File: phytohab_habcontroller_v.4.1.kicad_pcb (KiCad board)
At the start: 4 copper layers, 180.9 x 89.8 mm, 56 parts, among them J1 UMPT-02-01-L-RA-WT-M-TR, J10 I²C, J11 I²C, J12 I²C, J13 I²C, J14 I²C, J15 I²C, J2 HTSS-120-01-L-DV, J7 I²C, J8 I²C, J9 I²C, U101 DMP3037LSS-13, U301 MIC37100-3.3WS-TR, U501 DS3231M+TRL, U601 PCA9548ARGE

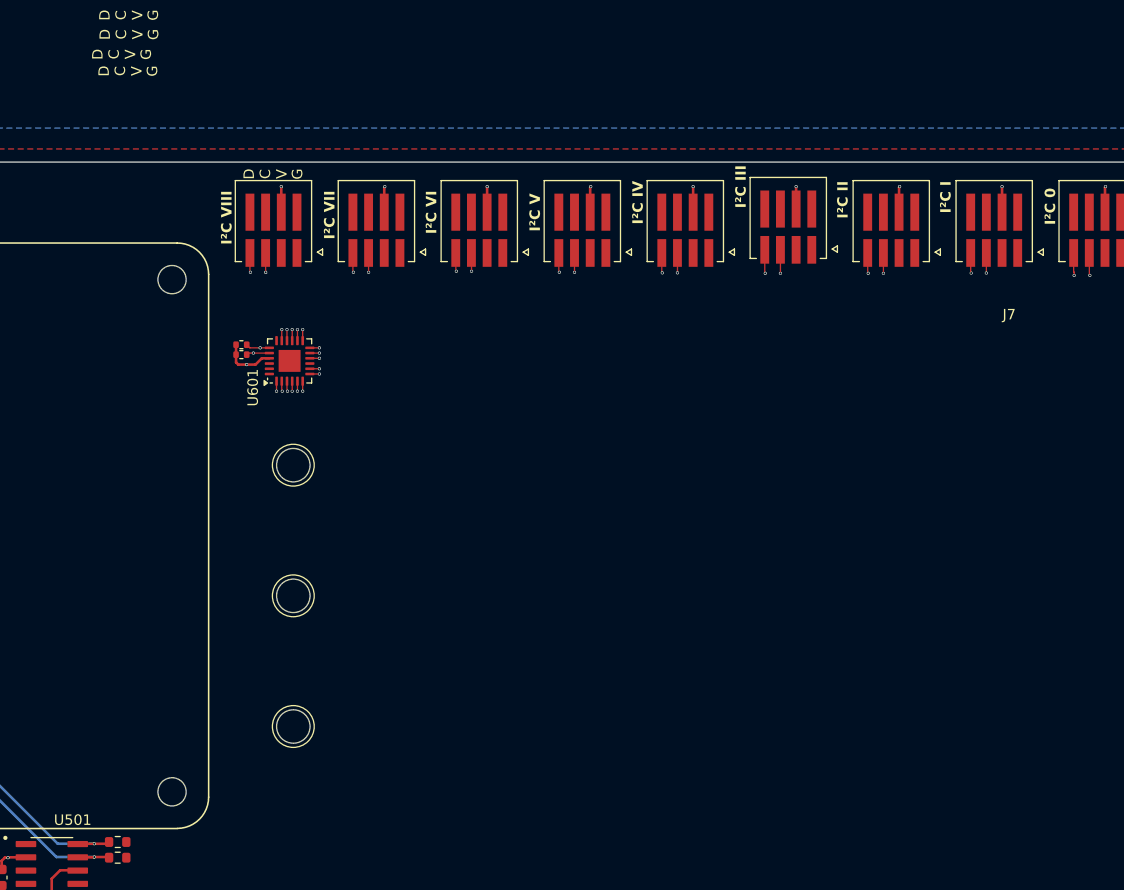
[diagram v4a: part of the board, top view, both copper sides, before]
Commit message: prepped for daughterboards
cons and mounting for GPIO-extension, I²C-ports cleaned up
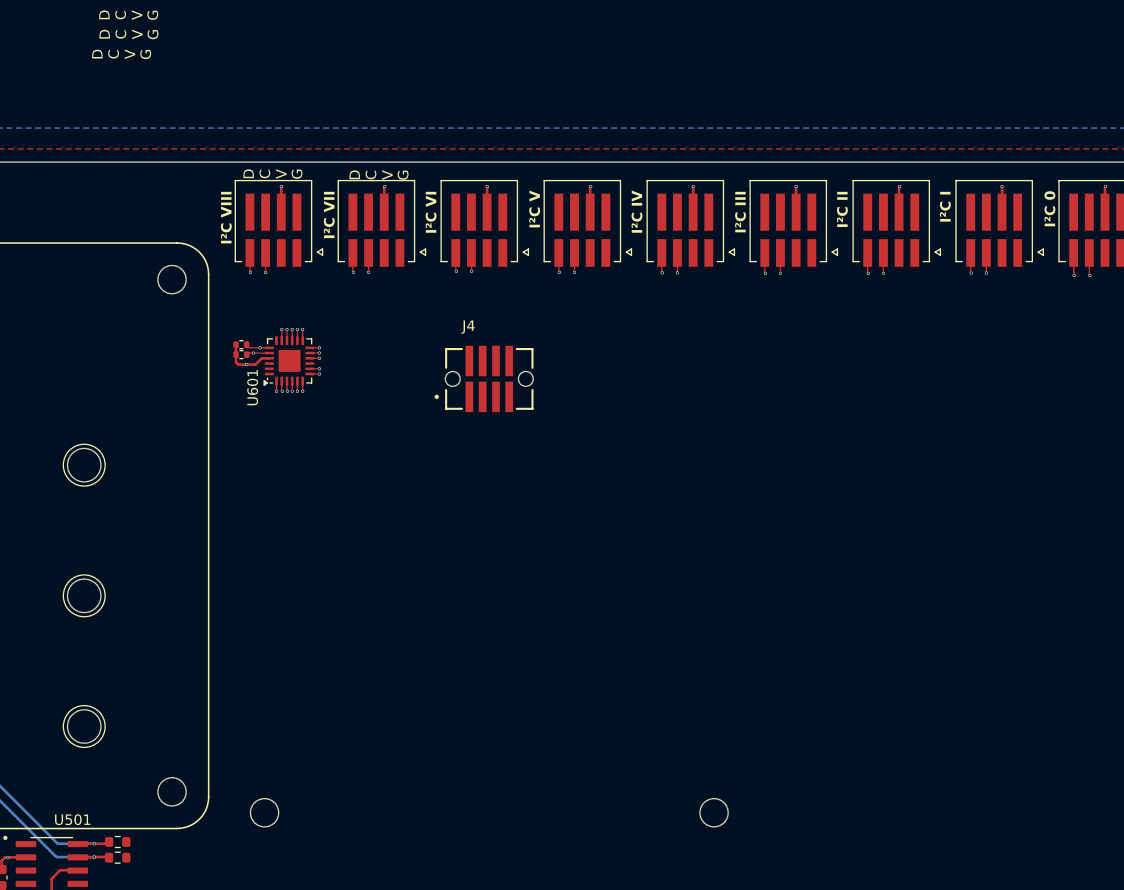
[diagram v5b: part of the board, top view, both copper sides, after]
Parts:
- added H2: MountingHole, MountingHole:MountingHole_2.7mm_M2.5_DIN965, F.Cu at (115.2, 84.5)
- added H6: MountingHole, MountingHole:MountingHole_2.7mm_M2.5_DIN965, F.Cu at (158.2, 84.5)
- added J4: TFM-104-02-L-D-A, connectors_SAMTEC:SAMTEC_TFM-104-02-L-D-A, F.Cu at (136.8, 43.0)
- moved DRA2 20.0 mm to (98.0, 63.8)
- moved J9 0.30 mm to (165.3, 27.9)
